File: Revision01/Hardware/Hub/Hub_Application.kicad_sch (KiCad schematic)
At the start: 81 parts, among them J10 IDC 6Pin Male Header, J11 IDC 6Pin Male Header, J12 IDC 6Pin Male Header, J13 IDC 6Pin Male Header, J14 IDC 6Pin Male Header, J15 IDC 6Pin Female Socket, J16 IDC 6Pin Male Header, J17 IDC 6Pin Female Socket, J18 IDC 6Pin Female Socket, J19 CON-SMA-EDGE-S, J6 IDC 6Pin Male Header, J7 IDC 6Pin Male Header, J8 IDC 6Pin Male Header, J9 IDC 6Pin Male Header, Q1 PMOS, Q2 NMOS, Q3 PMOS, U3 MPU-6500, U4 Adafruit 3070

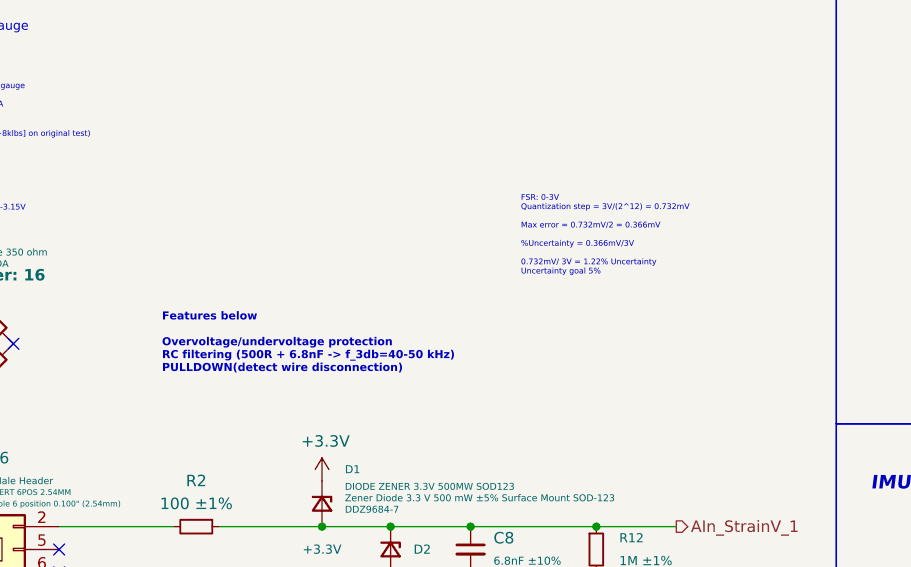
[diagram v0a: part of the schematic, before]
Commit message: improved documentation and small cosmetic changes - buck bypass resistor has X to indicate it is optional - RC documentation on schematic updated - Considering affects of 5V rail not being 5V 	- Lowers strainAmplifier offset 	- reduces strainAnalog signal
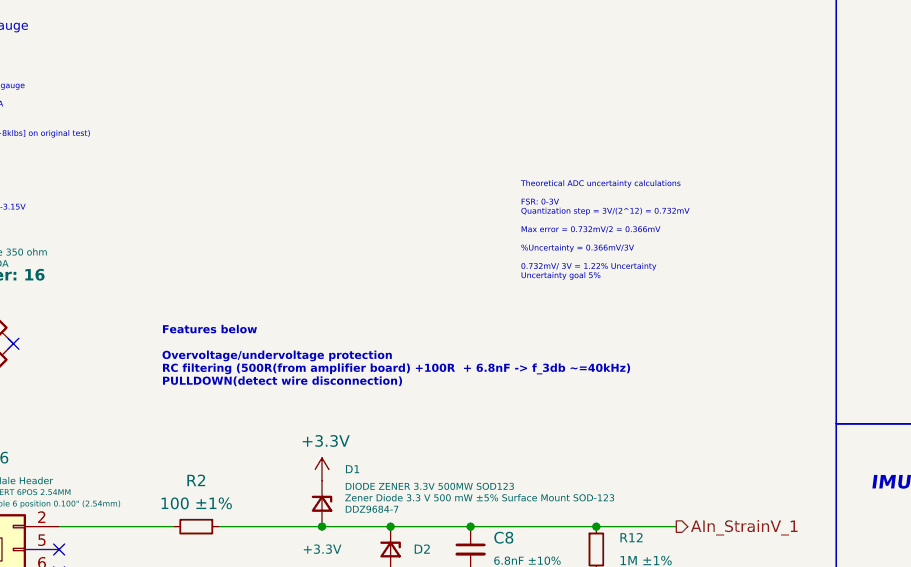
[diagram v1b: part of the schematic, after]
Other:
- note added: "Features below Overvoltage/undervoltage protection RC filtering (500R(from amplifier board) +100R + 6.8nF -> f_3db ~=40kHz) PULLDOWN(detect wire disconnection)"
- note added: "Theoretical ADC uncertainty calculations FSR: 0-3V Quantization step = 3V/(2^12) = 0.732mV Max error = 0.732mV/2 = 0.366mV %Uncertainty = 0.366mV/3V 0.732mV/ 3V = 1.22% Uncertainty Uncertainty goal 5%"
- note removed: "FSR: 0-3V Quantization step = 3V/(2^12) = 0.732mV Max error = 0.732mV/2 = 0.366mV %Uncertainty = 0.366mV/3V 0.732mV/ 3V = 1.22% Uncertainty Uncertainty goal 5%"
- note removed: "Features below Overvoltage/undervoltage protection RC filtering (500R + 6.8nF -> f_3db=40-50 kHz) PULLDOWN(detect wire disconnection)"
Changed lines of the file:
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@@
 		)
 	)
-	(text "Features below\n\nOvervoltage/undervoltage protection\nRC filtering (500R + 6.8nF -> f_3db=40-50 kHz)\nPULLDOWN(detect wire disconnection)"
+	(text "Features below\n\nOvervoltage/undervoltage protection\nRC filtering (500R(from amplifier board) +100R  + 6.8nF -> f_3db ~=40kHz)\nPULLDOWN(detect wire disconnection)"
 		(exclude_from_sim no)
-		(at 167.64 57.15 0)
+		(at 167.64 58.674 0)
 		(effects
 			(font
@@
 		)
 	)
-	(text "\nFSR: 0-3V\nQuantization step = 3V/(2^12) = 0.732mV\n\nMax error = 0.732mV/2 = 0.366mV\n\n%Uncertainty = 0.366mV/3V\n\n0.732mV/ 3V = 1.22% Uncertainty\nUncertainty goal 5%\n\n\n\n"
+	(text "Theoretical ADC uncertainty calculations\n\nFSR: 0-3V\nQuantization step = 3V/(2^12) = 0.732mV\n\nMax error = 0.732mV/2 = 0.366mV\n\n%Uncertainty = 0.366mV/3V\n\n0.732mV/ 3V = 1.22% Uncertainty\nUncertainty goal 5%\n\n\n\n"
 		(exclude_from_sim no)
 		(at 207.518 46.228 0)

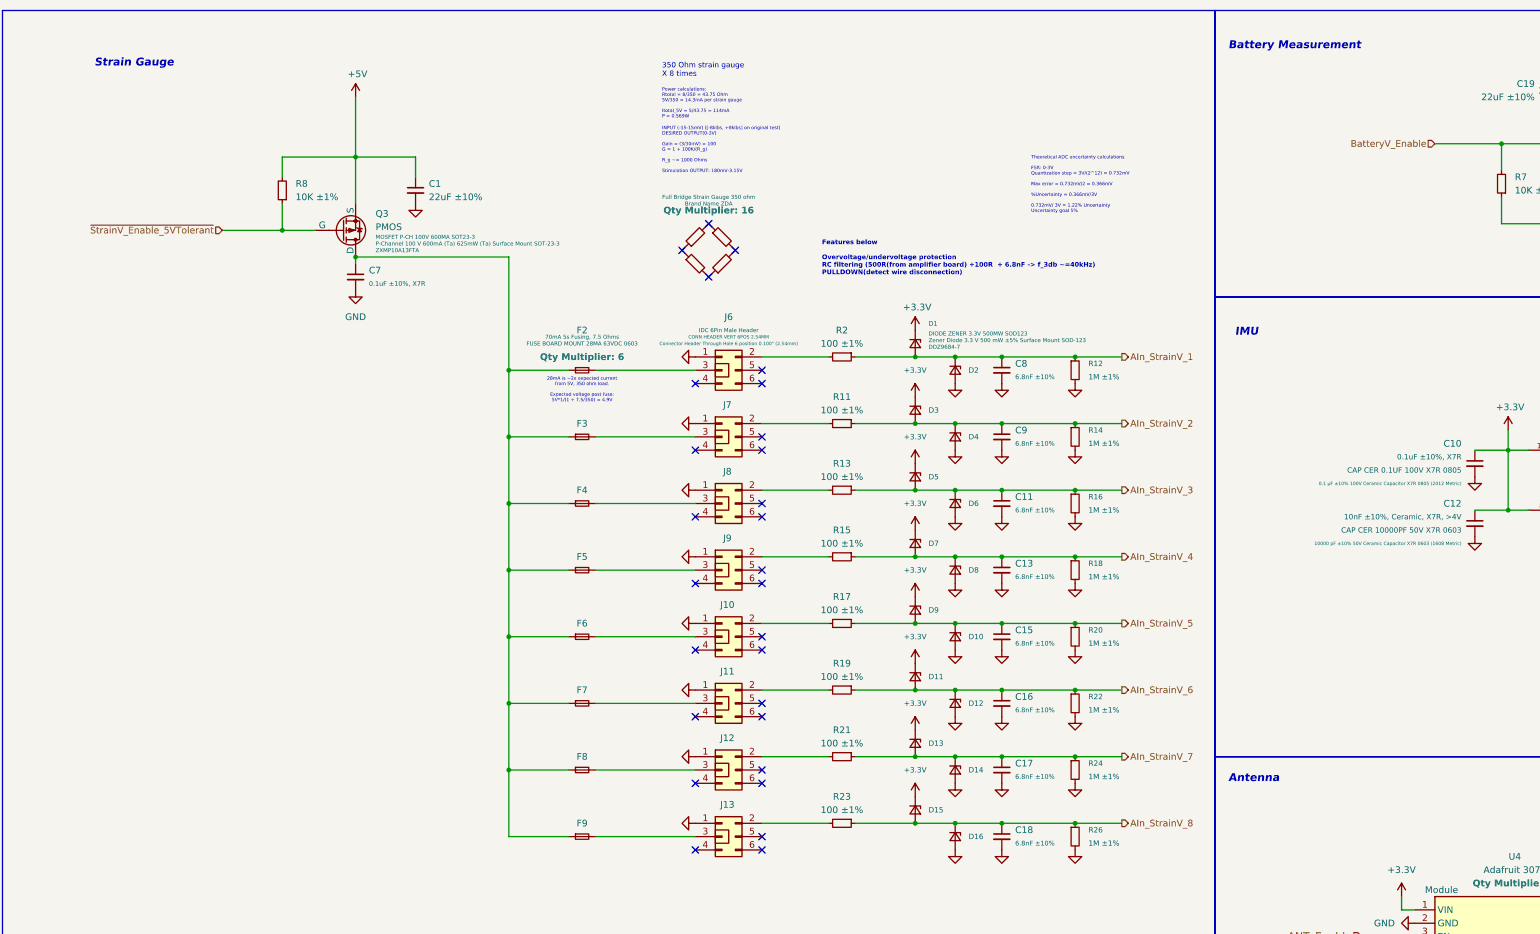
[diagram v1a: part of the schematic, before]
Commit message: Documentation cleanup
Added comments on current usage.
Cleaned up documentation folder as well as improved small details on it
Cleaned up old LTSPICE stimulations
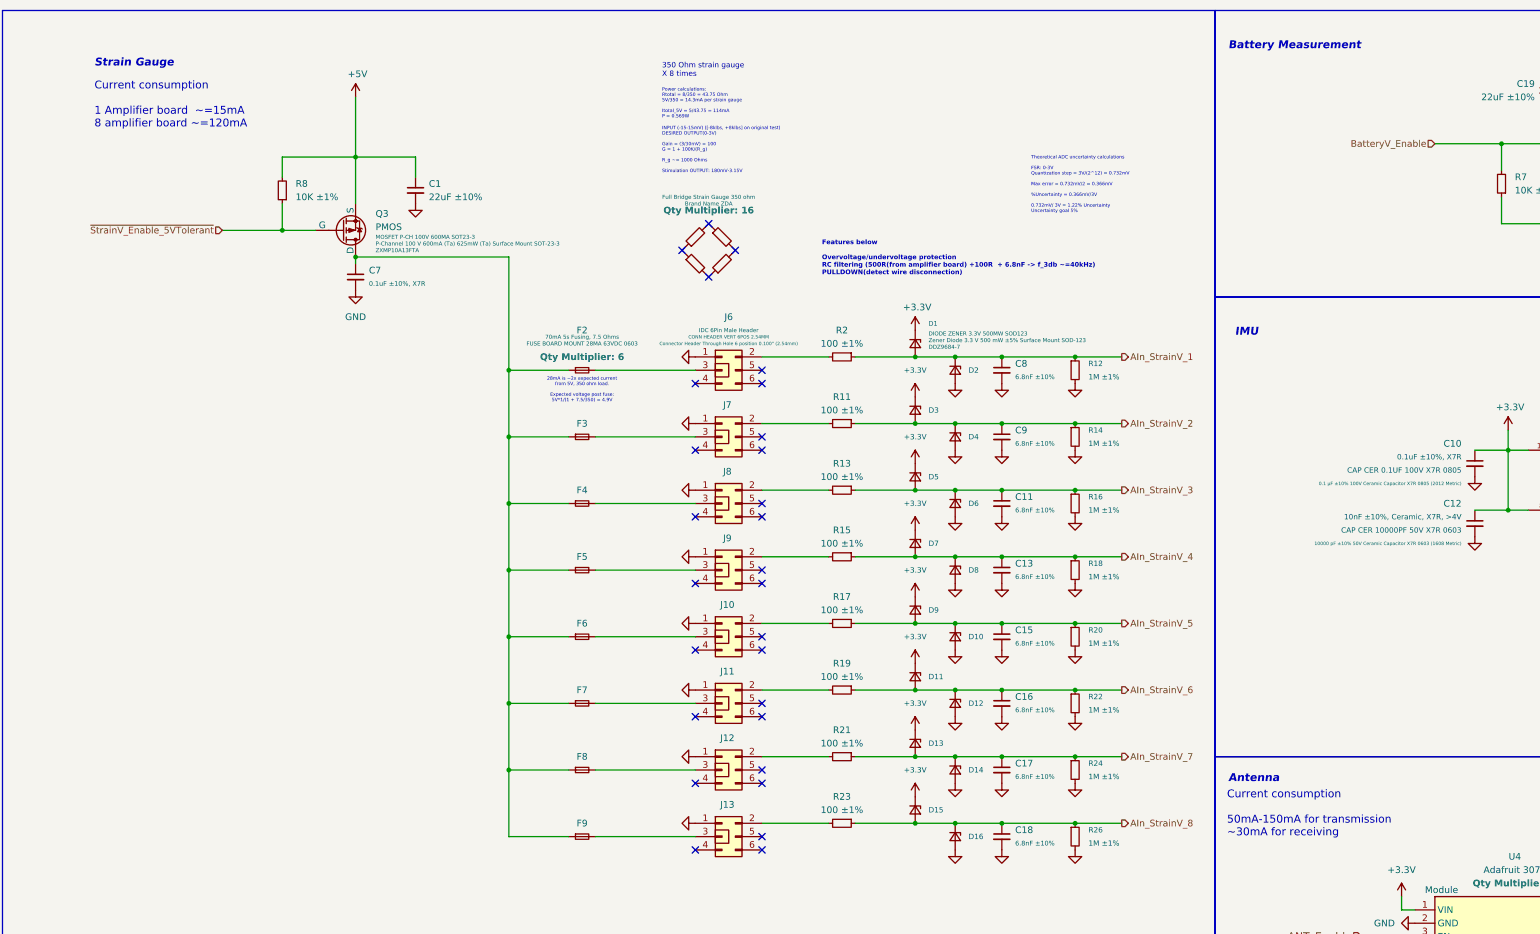
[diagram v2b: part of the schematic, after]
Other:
- note added: "Current consumption 1 Amplifier board ~=15mA 8 amplifier board ~=120mA"
- note added: "Current consumption 50mA-150mA for transmission ~30mA for receiving"
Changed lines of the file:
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@@
+		)
+	)
+	(text "Current consumption\n\n1 Amplifier board  ~=15mA \n8 amplifier board ~=120mA"
+		(exclude_from_sim no)
+		(at 28.956 29.464 0)
+		(effects
+			(font
+				(size 1.4986 1.4986)
+			)
+			(justify left)
 		)
 	)
@@
 		)
 	)
+	(text "Current consumption\n\n50mA-150mA for transmission\n~30mA for receiving"
+		(exclude_from_sim no)
+		(at 244.856 164.592 0)
+		(effects
+			(font
+				(size 1.4986 1.4986)
+			)
+			(justify left)
+		)
+	)

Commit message: neatened up silkscreen, added 0.1uF CAP to antenna
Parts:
- added C20: 0.1uF ±10%, X7R, Capacitor_SMD:C_0805_2012Metric_Pad1.18x1.45mm_HandSolder, symbol Device:C_Small
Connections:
- net +3.3V: now also C20.1
- net GND: now also C20.2
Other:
- moved on the sheet: AE1, J19, U4

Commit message: . Reverted Hardware/ changes to last known good commit f7a44a23fed9aca3ce7036a9f440c4d810a77518
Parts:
- removed C20: 0.1uF ±10%, X7R, Capacitor_SMD:C_0805_2012Metric_Pad1.18x1.45mm_HandSolder, symbol Device:C_Small
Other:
- note added: "FSR: 0-3V Quantization step = 3V/(2^12) = 0.732mV Max error = 0.732mV/2 = 0.366mV %Uncertainty = 0.366mV/3V 0.732mV/ 3V = 1.22% Uncertainty Uncertainty goal 5%"
- note added: "Features below Overvoltage/undervoltage protection RC filtering (500R + 6.8nF -> f_3db=40-50 kHz) PULLDOWN(detect wire disconnection)"
- note removed: "Current consumption 1 Amplifier board ~=15mA 8 amplifier board ~=120mA"
- note removed: "Current consumption 50mA-150mA for transmission ~30mA for receiving"
- note removed: "Features below Overvoltage/undervoltage protection RC filtering (500R(from amplifier board) +100R + 6.8nF -> f_3db ~=40kHz) PULLDOWN(detect wire disconnection)"
- note removed: "Theoretical ADC uncertainty calculations FSR: 0-3V Quantization step = 3V/(2^12) = 0.732mV Max error = 0.732mV/2 = 0.366mV %Uncertainty = 0.366mV/3V 0.732mV/ 3V = 1.22% Uncertainty Uncertainty goal 5%"
- moved on the sheet: AE1, J19, U4

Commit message: . Hub & Amp: Changed wiring standard to GND SIG GND GND PWR GND . Hub: Added GND plane to 3.3V . Hub: Moved 1M pulldown resistor . Hub & Amp: Adjusted thermal relief tolerances . Hub: Changed buck convertor layout so capacitors are inline with feedback pin . Hub: Added stitching vias . Hub & Amp: Changed font sizes, changed silkscreen to be oriented one way
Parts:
- added C20, C21, C24: 22uF ±10%, Capacitor_SMD:C_1206_3216Metric_Pad1.33x1.80mm_HandSolder, symbol Device:C_Small
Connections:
- net +3.3V: now also C24.1
- net +5V: now also C20.1, C21.1
- net AIn_StrainV_1: no longer R12.1
- net AIn_StrainV_2: no longer R14.1
- net AIn_StrainV_3: no longer R16.1
- net AIn_StrainV_4: no longer R18.1
- net AIn_StrainV_5: no longer R20.1
- net AIn_StrainV_6: no longer R22.1
- net AIn_StrainV_7: no longer R24.1
- net AIn_StrainV_8: no longer R26.1
- net GND: now also J10.3 (Pin_3), J10.4 (Pin_4), J10.6 (Pin_6), J11.3 (Pin_3), J11.4 (Pin_4), J11.6 (Pin_6), J12.3 (Pin_3), J12.4 (Pin_4), J12.6 (Pin_6), J13.3 (Pin_3), J13.4 (Pin_4), J13.6 (Pin_6), J6.3 (Pin_3), J6.4 (Pin_4), J6.6 (Pin_6), J7.3 (Pin_3), J7.4 (Pin_4), J7.6 (Pin_6), J8.3 (Pin_3), J8.4 (Pin_4), J8.6 (Pin_6), J9.3 (Pin_3), J9.4 (Pin_4), J9.6 (Pin_6), C20.2, C21.2, C24.2
- net at F6.2: now also J10.5 (Pin_5); no longer J10.3 (Pin_3)
- net at F3.2: now also J7.5 (Pin_5); no longer J7.3 (Pin_3)
- net at J7.2 (Pin_2), R11.2: now also R14.1
- net at J9.2 (Pin_2), R15.2: now also R18.1
- net at F5.2: now also J9.5 (Pin_5); no longer J9.3 (Pin_3)
- net at J6.2 (Pin_2), R2.2: now also R12.1
- net at F2.2: now also J6.5 (Pin_5); no longer J6.3 (Pin_3)
- net at J8.2 (Pin_2), R13.2: now also R16.1
- net at F4.2: now also J8.5 (Pin_5); no longer J8.3 (Pin_3)
- net at J13.2 (Pin_2), R23.2: now also R26.1
- net at J10.2 (Pin_2), R17.2: now also R20.1
- net at F9.2: now also J13.5 (Pin_5); no longer J13.3 (Pin_3)
- net at J16.4 (Pin_4): no longer J15.5 (Pin_5)
- net at J16.5 (Pin_5): now also J15.5 (Pin_5)
- net at J12.2 (Pin_2), R21.2: now also R24.1
- net at J11.2 (Pin_2), R19.2: now also R22.1
- net at F7.2: now also J11.5 (Pin_5); no longer J11.3 (Pin_3)
- net at F8.2: now also J12.5 (Pin_5); no longer J12.3 (Pin_3)
- no-connect marks 55 -> 31
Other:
- note added: "Features below Overvoltage/undervoltage protection RC filtering (600R + 6.8nF -> f_3db=40-50 kHz) PULLDOWN(detect wire disconnection)"
- note added: "Full Load Power Cable Voltage RDS(ON) = 1.5 ohm R(eq) = 1/(8/(7.5 + 350)) ohm R(eq) = 44.7 ohm I(Full) = V/R = 5 / (1.5 + 44.7) I(Full) = 108mA V(Drain) = 5 - I(Full)*1.5 ohm = 4.838 V V(Cable) = (4.838V) - 1/8*I(Full)*7.5 ohm V(Cable) = 4.73675 V (94.7%) Full Load Bypass Capacitor Sag f(on) = 1khz t(on) = 100 us (10% of 1/f(on)) V(Drop) = (1/C)*I(Full)*t = (1/(20uF*3))*(108mA)*(100us) V(Drop) = 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"
- note removed: "28mA is ~2x expected current from 5V, 350 ohm load. Expected voltage post fuse: 5V*1/(1 + 7.5/350) = 4.9V"
- note removed: "Features below Overvoltage/undervoltage protection RC filtering (500R + 6.8nF -> f_3db=40-50 kHz) PULLDOWN(detect wire disconnection)"
- moved on the sheet: AE1, C1, F2, F3, F4, F5, F6, F7, F8, F9, J19, R12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

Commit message: . Changed battery measurement switch to 1/5 1/2 mA, uses the same components as the regular analog in chain . Added simulation for battery measurement "switch" . Checked DRC & ERC
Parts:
- removed C19: 22uF ±10%, Capacitor_SMD:C_1206_3216Metric_Pad1.33x1.80mm_HandSolder, symbol Device:C_Small
- removed Q1: PMOS, Package_TO_SOT_SMD:TSOT-23, symbol Simulation_SPICE:PMOS
- removed Q2: NMOS, Package_TO_SOT_SMD:TSOT-23, symbol Simulation_SPICE:NMOS
- added D17, D18: D_Zener_Small, Diode_SMD:D_SOD-123, symbol Device:D_Zener_Small
- added R25: 10K ±1%, Resistor_SMD:R_0805_2012Metric_Pad1.20x1.40mm_HandSolder, symbol Device:R_Small
- C6: value 0.1uF ±10%, X7R -> 6.8nF ±10%; footprint Capacitor_SMD:C_0805_2012Metric_Pad1.18x1.45mm_HandSolder -> Capacitor_SMD:C_0603_1608Metric_Pad1.08x0.95mm_HandSolder; Detailed Description 0.1 µF ±10% 100V Ceramic Capacitor X7R 0805 (2012 Metric) -> Multilayer Ceramic Capacitors MLCC - SMD/SMT 6.8nF+/-10% 50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; DigiKey Link https://www.digikey.ca/en/products/detail/samsung-electro-mechanics/CL21B104KCFNNNE/5961324 -> https://www.digikey.ca/en/products/detail/samsung-electro-mechanics/CL10B682KB8NNNC/3886843?s=N4IgTCBcDaIMIBkCMAGAQgNgBxgNJqwDli4QBdAXyA; DigiKey Part Number 1276-6840-1-ND -> 1276-1185-2-ND; Manufacturer Part Number CL21B104KCFNNNE -> CL10B682KB8NNNC; Mouser Link https://www.mouser.ca/ProductDetail/Samsung-Electro-Mechani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 -> https://mou.sr/3J8ffq3; Mouser Part Number 187-CL21B104KCFNNNE -> 187-CL10B682KB8NNNC; Package 0805 (2012 Metric) -> 0603 (1608 metric)
- R6: value 15K ±1% -> 10K ±1%; Detailed Description 15 kOhms ±1% 0.125W, 1/8W Chip Resistor 0805 (2012 Metric) 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 -> 10 kOhms ±1% 0.125W, 1/8W Chip Resistor 0805 (2012 Metric) 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; DigiKey Link https://www.digikey.ca/en/products/detail/vishay-dale/CRCW080515K0FKEA/1175769 -> https://www.digikey.ca/en/products/detail/vishay-dale/CRCW080510K0FKEA/1175751; DigiKey Part Number 541-15.0KCCT-ND -> 541-10.0KCCT-ND; Manufacturer Part Number CRCW080515K0FKEA -> CRCW080510K0FKEA; Mouser Link https://www.mouser.ca/ProductDetail/Vishay/CRCW080515K0FKEA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 -> https://www.mouser.ca/ProductDetail/Vishay/CRCW080510K0FKEA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; Mouser Part Number 71-CRCW0805-15K-E3 -> 71-CRCW0805-10K-E3
- R9: value 5K ±1% -> 10K ±1%; Detailed Description 5 kOhms ±1% 0.125W, 1/8W Chip Resistor 0805 (2012 Metric) A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 -> 10 kOhms ±1% 0.125W, 1/8W Chip Resistor 0805 (2012 Metric) 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; DigiKey Link https://www.digikey.ca/en/products/detail/vishay-dale/CRCW08055K00FKTA/5075661 -> https://www.digikey.ca/en/products/detail/vishay-dale/CRCW080510K0FKEA/1175751; DigiKey Part Number 541-CRCW08055K00FKTACT-ND -> 541-10.0KCCT-ND; Manufacturer Part Number CRCW08055K00FKTA -> CRCW080510K0FKEA; Mouser Link https://www.mouser.ca/ProductDetail/Vishay/CRCW08055K00FKTA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 -> https://www.mouser.ca/ProductDetail/Vishay/CRCW080510K0FKEA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; Mouser Part Number 71-CRCW0805-5K -> 71-CRCW0805-10K-E3
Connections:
- net BatteryV_Enable is gone; now on an unnamed net: R7.2
- net +3.3V: now also D17.1 (K)
- net AIn_BatteryV: now also R6.2, R7.1, D17.2 (A), D18.1 (K); no longer R6.1
- net GND: now also R6.1, D18.2 (A); no longer R7.1
- net ~{StrainV_Enable_5VTolerant}: now also R25.2; no longer Q3.2 (G)
- new net: Q3.2 (G), R25.1
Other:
- note added: "1/5 divider. 0.6mA @ 15V 0V if no VBattery (usb-receiver)"
- note removed: "Calculation for battery measurement: Battery range is from 4.5-12V. Chosen resistors 5 and 15k. Left extra room in resistor values for uncertainty Vmax = 3V Vmin = 1.125V"
- note removed: "For a PMOS CUTOFF REGION - Vsg < Vth SATURATION REGION - Vsg > Vth"
- note removed: "V_th_min = -0.7V"
- note removed: "V_th_min = 0.8V"
- moved on the sheet: R8
